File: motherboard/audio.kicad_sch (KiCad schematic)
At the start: 1 part, among them U23 TPA2028D1YZFT

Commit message: audio done
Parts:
- added C71, C72: 0.1uF, Capacitor_SMD:C_0402_1005Metric, symbol Device:C_Small
- added C73, C75, C76, C78, C79: 1uF, Capacitor_SMD:C_0402_1005Metric, symbol Device:C_Small
- added C74, C77: 10uF, Capacitor_SMD:C_0402_1005Metric, symbol Device:C_Small
- added CN1: PJ-332A-6A (3.5mm Jack), Headphone_Jack:AUDIO-SMD_PJ-332A-6A, symbol Headphone_Jack:PJ-332A-6A
- added D6, D7: LESD8D5.0CB1T5G, Diode_SMD:D_SOD-882, symbol Device:D_TVS_Small_Filled
- added J3: RIGHT SPEAKERS, symbol Connector_Generic:Conn_01x02
- added J4: LEFT SPEAKERS, symbol Connector_Generic:Conn_01x02
- added Q12: 2SK3018W, Package_TO_SOT_SMD:SOT-323_SC-70, symbol Transistor_FET:BSS214NW
- added R102, R103, R104: 0R, Resistor_SMD:R_0402_1005Metric, symbol Device:R_Small
- added R105, R106, R110: 10k, Resistor_SMD:R_0402_1005Metric, symbol Device:R_Small
- added R107, R108: 33R, Resistor_SMD:R_0402_1005Metric, symbol Device:R_Small
- added R109: 100k, Resistor_SMD:R_0402_1005Metric, symbol Device:R_Small
- added R111: 2.2k, Resistor_SMD:R_0402_1005Metric, symbol Device:R_Small
- added U25: TPA2028D1YZFT, TPA2028D1YZFT:BGA9C50P3X3_162X162X63, symbol Audio_Amp:TPA2028D1YZFT
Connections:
- net GND: now reaches U23.A1 (PGND)
- net GND: now also C73.2, C74.2, C76.1, C77.2, C79.1, D6.1 (A1), D7.1 (A1), Q12.2 (S), U25.A1 (PGND)
- net R_AMP_SCL: now reaches U23.A2 (SCL)
- net R_AMP_SDA: now reaches U23.A3 (SDA)
- net at U23.B1 (OUT+): now also J3.1 (Pin_1)
- net SPK_EN: now reaches U23.B2 (EN)
- net SPK_EN: now also U25.B2 (EN)
- net at U23.B3 (IN+): now also C75.2
- net at U23.C1 (OUT-): now also J3.2 (Pin_2)
- net +5V: now reaches U23.C2 (PVDD)
- net +5V: now also C74.1, C77.1, U25.C2 (PVDD)
- net at U23.C3 (IN-): now also C76.2
- new net: C72.2, R107.2
- new net: C73.1, Q12.1 (G), R110.1
- new net: J4.1 (Pin_1), U25.B1 (OUT+)
- new net: C78.2, U25.B3 (IN+)
- new net: J4.2 (Pin_2), U25.C1 (OUT-)
- new net: C79.2, U25.C3 (IN-)
- new net: C71.2, R108.2
- new net +1V8: R109.2, R111.2
- new net GND_AUDUO: CN1.2, R105.1, R106.1, R107.1, R108.1
- new net GPIO1_C4/HP_DET_L: Q12.3 (D), R111.1
- new net HPL: C72.1, R104.2, R106.2
- new net HPR: C71.1, R103.2, R105.2
- new net L_AMP_SCL: U25.A2 (SCL)
- new net L_AMP_SDA: U25.A3 (SDA)
- new net L_DET: CN1.5, CN1.6, R109.1, R110.2
- new net L_HP: C78.1, CN1.4, D7.2 (A2), R104.1
- new net MIC: CN1.1, R102.1
- new net MIC_IN: R102.2
- new net R_HP: C75.1, CN1.3, D6.2 (A2), R103.1

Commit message: motherboard schematic done
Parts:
- added R118, R119: 0R, Resistor_SMD:R_0402_1005Metric, symbol Device:R_Small
- J3, J4: footprint (none) -> Connector_PinHeader_2.54mm:PinHeader_1x02_P2.54mm_Horizontal
- U23, U25: footprint TPA2028D1YZFT:BGA9C50P3X3_162X162X63 -> Audio_Amp:BGA9C50P3X3_162X162X63
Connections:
- net HPL: now also C78.1
- net HPR: now also C75.1
- net L_HP: no longer C78.1
- net R_HP: no longer C75.1
- net SPK_EN: now also R118.1, R118.2, R119.1; no longer U25.B2 (EN)
- new net: R119.2, U25.B2 (EN)
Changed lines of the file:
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@@
 	(wire
 		(pts
-			(xy 151.13 134.62) (xy 161.29 134.62)
+			(xy 151.13 134.62) (xy 167.64 134.62)
 		)
 		(stroke
@@
 	(wire
 		(pts
-			(xy 80.01 81.28) (xy 87.63 81.28)
+			(xy 68.58 88.9) (xy 72.39 88.9)
 		)
 		(stroke
@@
 	(wire
 		(pts
+			(xy 81.28 81.28) (xy 87.63 81.28)
+		)
+		(stroke
+			(width 0)
+			(type default)
+		)
+	)
+	(wire
+		(pts
 			(xy 135.89 113.03) (xy 138.43 113.03)
 		)
@@
 	(wire
 		(pts
+			(xy 77.47 88.9) (xy 81.28 88.9)
+		)
+		(stroke
+			(width 0)
+			(type default)
+		)
+	)
+	(wire
+		(pts
 			(xy 88.9 127) (xy 99.06 127)
 		)
@@
 	(wire
 		(pts
-			(xy 156.21 127) (xy 161.29 127)
+			(xy 156.21 127) (xy 167.64 127)
 		)
 		(stroke
@@
 	(wire
 		(pts
+			(xy 81.28 88.9) (xy 81.28 81.28)
+		)
+		(stroke
+			(width 0)
+			(type default)
+		)
+	)
+	(wire
+		(pts
+			(xy 172.72 91.44) (xy 175.26 91.44)
+		)
+		(stroke
+			(width 0)
+			(type default)
+		)
+	)
+	(wire
+		(pts
 			(xy 132.08 134.62) (xy 151.13 134.62)
 		)
@@
 	(wire
 		(pts
+			(xy 175.26 85.09) (xy 179.07 85.09)
+		)
+		(stroke
+			(width 0)
+			(type default)
+		)
+	)
+	(wire
+		(pts
 			(xy 99.06 148.59) (xy 100.33 148.59)
 		)
@@
 	(wire
 		(pts
+			(xy 175.26 91.44) (xy 175.26 85.09)
+		)
+		(stroke
+			(width 0)
+			(type default)
+		)
+	)
+	(wire
+		(pts
 			(xy 88.9 129.54) (xy 95.25 129.54)
 		)
@@
 	(wire
 		(pts
-			(xy 171.45 85.09) (xy 179.07 85.09)
+			(xy 157.48 91.44) (xy 167.64 91.44)
 		)
 		(stroke
@@
 		)
 	)
-	(label "L_HP"
+	(label "L_AUDIO"
 		(at 160.02 77.47 0)
 		(fields_autoplaced yes)
@@
 		)
 	)
-	(label "R_HP"
-		(at 68.58 73.66 0)
+	(label "SPK_EN"
+		(at 157.48 91.44 0)
 		(fields_autoplaced yes)
 		(effects
@@
 		)
 	)
-	(label "SPK_EN"
-		(at 171.45 85.09 0)
+	(label "AGND"
+		(at 93.98 137.16 180)
 		(fields_autoplaced yes)
 		(effects
@@
 				(size 1.27 1.27)
 			)
-			(justify left bottom)
+			(justify right bottom)
 		)
 	)
-	(label "AGND"
-		(at 93.98 137.16 180)
+	(label "L_AUDIO"
+		(at 157.48 134.62 0)
 		(fields_autoplaced yes)
 		(effects
@@
 				(size 1.27 1.27)
 			)
-			(justify right bottom)
+			(justify left bottom)
 		)
 	)
@@
 	)
 	(label "SPK_EN"
-		(at 80.01 81.28 0)
+		(at 81.28 81.28 0)
+		(fields_autoplaced yes)
+		(effects
+			(font
+				(size 1.27 1.27)
+			)
+			(justify left bottom)
+		)
+	)
+	(label "R_AUDIO"
+		(at 157.48 127 0)
 		(fields_autoplaced yes)
 		(effects
@@
 		)
 	)
+	(label "R_AUDIO"
+		(at 68.58 73.66 0)
+		(fields_autoplaced yes)
+		(effects
+			(font
+				(size 1.27 1.27)
+			)
+			(justify left bottom)
+		)
+	)
 	(label "R_DET"
 		(at 111.76 111.76 0)
@@
 	(hierarchical_label "SPK_EN"
 		(shape input)
-		(at 80.01 81.28 180)
+		(at 68.58 88.9 180)
 		(fields_autoplaced yes)
 		(effects
@@
 	(hierarchical_label "HPR"
 		(shape input)
-		(at 161.29 127 0)
+		(at 167.64 127 0)
 		(fields_autoplaced yes)
 		(effects
@@
 	(hierarchical_label "HPL"
 		(shape input)
-		(at 161.29 134.62 0)
+		(at 167.64 134.62 0)
 		(fields_autoplaced yes)
 		(effects
@@
 			)
 		)
-		(property "Footprint" ""
+		(property "Footprint" "Connector_PinHeader_2.54mm:PinHeader_1x02_P2.54mm_Horizontal"
 			(at 125.73 68.58 0)
 			(effects
@@
 			)
 		)
-		(property "Footprint" "TPA2028D1YZFT:BGA9C50P3X3_162X162X63"
+		(property "Footprint" "Audio_Amp:BGA9C50P3X3_162X162X63"
 			(at 195.58 77.47 0)
 			(effects
@@
 			)
 		)
-		(property "Footprint" "TPA2028D1YZFT:BGA9C50P3X3_162X162X63"
+		(property "Footprint" "Audio_Amp:BGA9C50P3X3_162X162X63"
 			(at 104.14 73.66 0)
 			(effects
@@
 			)
 		)
-		(property "Footprint" ""
+		(property "Footprint" "Connector_PinHeader_2.54mm:PinHeader_1x02_P2.54mm_Horizontal"
 			(at 217.17 72.39 0)
 			(effects
@@
 	)
 	(symbol
+		(lib_id "Device:R_Small")
+		(at 170.18 91.44 90)
+		(unit 1)
+		(exclude_from_sim no)
+		(in_bom yes)
+		(on_board yes)
+		(dnp no)
+		(fields_autoplaced yes)
+		(property "Reference" "R119"
+			(at 170.18 86.36 90)
+			(effects
+				(font
+					(size 1.27 1.27)
+				)
+			)
+		)
+		(property "Value" "0R"
+			(at 170.18 88.9 90)
+			(effects
+				(font
+					(size 1.27 1.27)
+				)
+			)
+		)
+		(property "Footprint" "Resistor_SMD:R_0402_1005Metric"
+			(at 170.18 91.44 0)
+			(effects
+				(font
+					(size 1.27 1.27)
+				)
+				(hide yes)
+			)
+		)
+		(property "Datasheet" "~"
+			(at 170.18 91.44 0)
+			(effects
+				(font
+					(size 1.27 1.27)
+				)
+				(hide yes)
+			)
+		)
+		(property "Description" "Resistor, small symbol"
+			(at 170.18 91.44 0)
+			(effects
+				(font
+					(size 1.27 1.27)
+				)
+				(hide yes)
+			)
+		)
+		(pin "1"
+		)
+		(pin "2"
+		)
+		(instances
+			(project "motherboard"
+				(path "/025fe4d1-0305-4b34-be04-f8d9818125a4/d168cefe-cdbf-401a-9d73-1a46286dd06c"
+					(reference "R119")
+					(unit 1)
+				)
+			)
+		)
+	)
+	(symbol
 		(lib_id "power:GND")
 		(at 160.02 80.01 0)
@@
 					(unit 1)
 				)
+			)
+		)
+	)
+	(symbol
+		(lib_id "Device:R_Small")
+		(at 74.93 88.9 90)
+		(unit 1)
+		(exclude_from_sim no)
+		(in_bom yes)
+		(on_board yes)
+		(dnp no)
+		(fields_autoplaced yes)
+		(property "Reference" "R118"
+			(at 74.93 83.82 90)
+			(effects
+				(font
+					(size 1.27 1.27)
+				)
+			)
+		)
+		(property "Value" "0R"
+			(at 74.93 86.36 90)
+			(effects
+				(font
+					(size 1.27 1.27)
+				)
+			)
+		)
+		(property "Footprint" "Resistor_SMD:R_0402_1005Metric"
+			(at 74.93 88.9 0)
+			(effects
+				(font
+					(size 1.27 1.27)
+				)
+				(hide yes)
+			)
+		)
+		(property "Datasheet" "~"
+			(at 74.93 88.9 0)
+			(effects
+				(font
+					(size 1.27 1.27)
+				)
+				(hide yes)
+			)
+		)
+		(property "Description" "Resistor, small symbol"
+			(at 74.93 88.9 0)
+			(effects
+				(font
+					(size 1.27 1.27)
+				)
+				(hide yes)
+			)
+		)
+		(pin "1"
+		)
+		(pin "2"
+		)
+		(instances
+			(project "motherboard"
+				(path "/025fe4d1-0305-4b34-be04-f8d9818125a4/d168cefe-cdbf-401a-9d73-1a46286dd06c"
+					(reference "R118")
+					(unit 1)
+				)

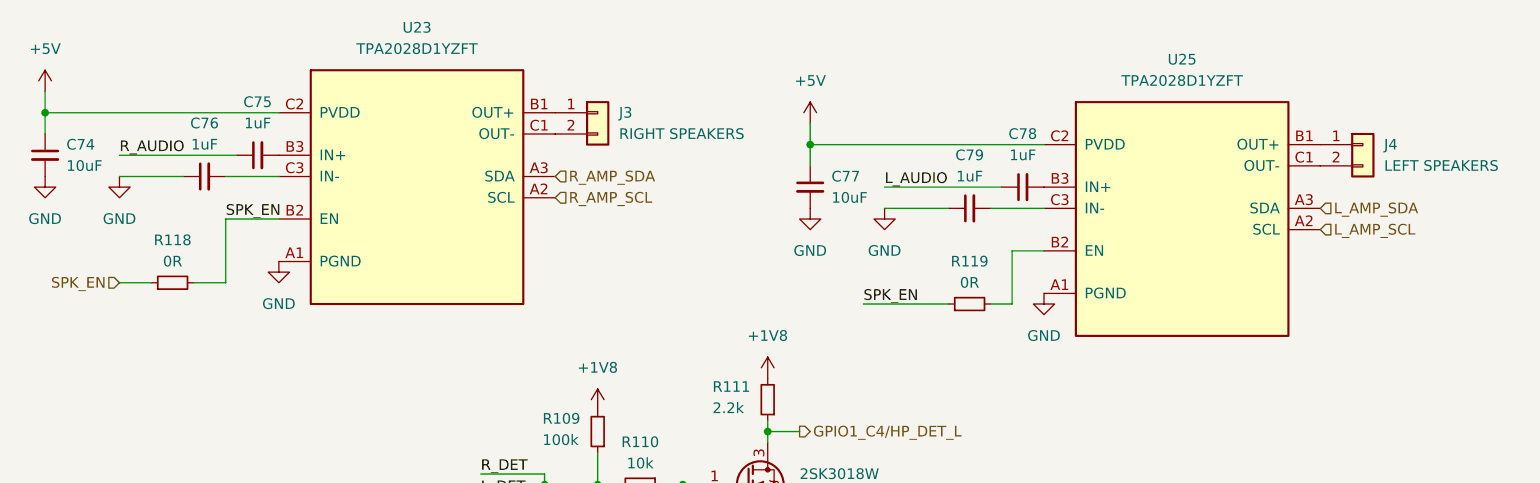
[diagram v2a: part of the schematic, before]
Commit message: placement roughly halfway done
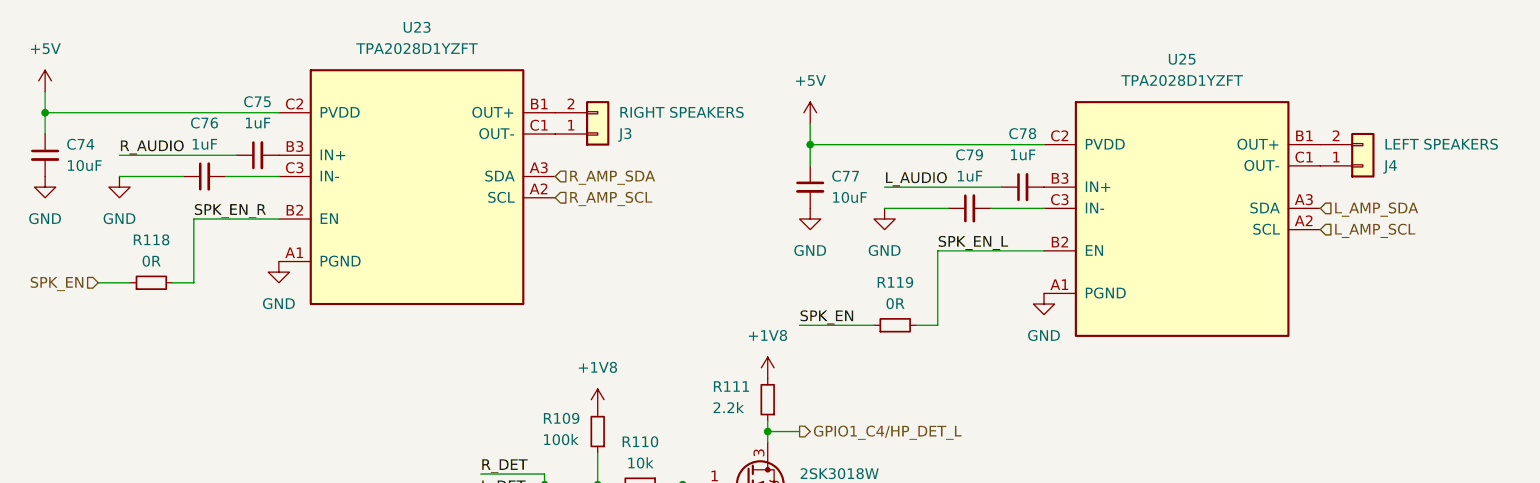
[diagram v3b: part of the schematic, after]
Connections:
- net SPK_EN: no longer R118.2, U23.B2 (EN)
- net at J3.1 (Pin_1): now also U23.C1 (OUT-); no longer U23.B1 (OUT+)
- net at J3.2 (Pin_2): now also U23.B1 (OUT+); no longer U23.C1 (OUT-)
- net at U25.B1 (OUT+): now also J4.2 (Pin_2); no longer J4.1 (Pin_1)
- net SPK_EN_L: now reaches R119.2, U25.B2 (EN)
- net at U25.C1 (OUT-): now also J4.1 (Pin_1); no longer J4.2 (Pin_2)
- new net SPK_EN_R: R118.2, U23.B2 (EN)
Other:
- moved on the sheet: R118, R119
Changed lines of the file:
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@@
 	(wire
 		(pts
+			(xy 77.47 81.28) (xy 77.47 88.9)
+		)
+		(stroke
+			(width 0)
+			(type default)
+		)
+	)
+	(wire
+		(pts
 			(xy 153.67 147.32) (xy 156.21 147.32)
 		)
@@
 	(wire
 		(pts
-			(xy 68.58 88.9) (xy 72.39 88.9)
+			(xy 77.47 88.9) (xy 74.93 88.9)
 		)
 		(stroke
@@
 	(wire
 		(pts
-			(xy 128.27 113.03) (xy 125.73 113.03)
+			(xy 66.04 88.9) (xy 69.85 88.9)
 		)
 		(stroke
@@
 	(wire
 		(pts
-			(xy 81.28 81.28) (xy 87.63 81.28)
+			(xy 128.27 113.03) (xy 125.73 113.03)
 		)
 		(stroke
@@
 	(wire
 		(pts
-			(xy 135.89 113.03) (xy 138.43 113.03)
+			(xy 77.47 81.28) (xy 87.63 81.28)
 		)
 		(stroke
@@
 	(wire
 		(pts
-			(xy 101.6 134.62) (xy 116.84 134.62)
+			(xy 135.89 113.03) (xy 138.43 113.03)
 		)
 		(stroke
@@
 	(wire
 		(pts
-			(xy 99.06 142.24) (xy 99.06 148.59)
+			(xy 101.6 134.62) (xy 116.84 134.62)
 		)
 		(stroke
@@
 	(wire
 		(pts
-			(xy 151.13 134.62) (xy 151.13 135.89)
+			(xy 99.06 142.24) (xy 99.06 148.59)
 		)
 		(stroke
@@
 	(wire
 		(pts
-			(xy 151.13 74.93) (xy 151.13 72.39)
+			(xy 151.13 134.62) (xy 151.13 135.89)
 		)
 		(stroke
@@
 	(wire
 		(pts
-			(xy 77.47 88.9) (xy 81.28 88.9)
+			(xy 151.13 74.93) (xy 151.13 72.39)
 		)
 		(stroke
@@
 	(wire
 		(pts
-			(xy 81.28 88.9) (xy 81.28 81.28)
-		)
-		(stroke
-			(width 0)
-			(type default)
-		)
-	)
-	(wire
-		(pts
-			(xy 172.72 91.44) (xy 175.26 91.44)
+			(xy 163.83 93.98) (xy 166.37 93.98)
 		)
 		(stroke
@@
 	(wire
 		(pts
-			(xy 175.26 85.09) (xy 179.07 85.09)
+			(xy 166.37 85.09) (xy 179.07 85.09)
 		)
 		(stroke
@@
 	(wire
 		(pts
-			(xy 175.26 91.44) (xy 175.26 85.09)
+			(xy 166.37 93.98) (xy 166.37 85.09)
 		)
 		(stroke
@@
 	(wire
 		(pts
-			(xy 157.48 91.44) (xy 167.64 91.44)
+			(xy 134.62 142.24) (xy 134.62 140.97)
 		)
 		(stroke
@@
 	(wire
 		(pts
-			(xy 134.62 142.24) (xy 134.62 140.97)
+			(xy 121.92 127) (xy 134.62 127)
 		)
 		(stroke
@@
 	(wire
 		(pts
-			(xy 121.92 127) (xy 134.62 127)
+			(xy 149.86 93.98) (xy 158.75 93.98)
 		)
 		(stroke
@@
 	)
 	(label "SPK_EN"
-		(at 157.48 91.44 0)
+		(at 149.86 93.98 0)
 		(fields_autoplaced yes)
 		(effects
@@
 		)
 	)
-	(label "SPK_EN"
-		(at 81.28 81.28 0)
+	(label "SPK_EN_R"
+		(at 77.47 81.28 0)
 		(fields_autoplaced yes)
 		(effects
@@
 		)
 	)
+	(label "SPK_EN_L"
+		(at 166.37 85.09 0)
+		(fields_autoplaced yes)
+		(effects
+			(font
+				(size 1.27 1.27)
+			)
+			(justify left bottom)
+		)
+	)
 	(label "R_DET"
 		(at 111.76 111.76 0)
@@
 	(hierarchical_label "SPK_EN"
 		(shape input)
-		(at 68.58 88.9 180)
+		(at 66.04 88.9 180)
 		(fields_autoplaced yes)
 		(effects
@@
 	(symbol
 		(lib_id "Connector_Generic:Conn_01x02")
-		(at 125.73 68.58 0)
+		(at 125.73 71.12 0)
+		(mirror x)
 		(unit 1)
 		(exclude_from_sim no)
@@
 		(on_board yes)
 		(dnp no)
-		(fields_autoplaced yes)
 		(property "Reference" "J3"
-			(at 128.27 68.5799 0)
+			(at 128.27 71.1201 0)
 			(effects
 				(font
@@
 		)
 		(property "Value" "RIGHT SPEAKERS"
-			(at 128.27 71.1199 0)
+			(at 128.27 68.5801 0)
 			(effects
 				(font
@@
 		)
 		(property "Footprint" "Connector_PinHeader_2.54mm:PinHeader_1x02_P2.54mm_Horizontal"
-			(at 125.73 68.58 0)
+			(at 125.73 71.12 0)
 			(effects
 				(font
@@
 		)
 		(property "Datasheet" "~"
-			(at 125.73 68.58 0)
+			(at 125.73 71.12 0)
 			(effects
 				(font
@@
 		)
 		(property "Description" "Generic connector, single row, 01x02, script generated (kicad-library-utils/schlib/autogen/connector/)"
-			(at 125.73 68.58 0)
+			(at 125.73 71.12 0)
 			(effects
 				(font
@@
 	(symbol
 		(lib_id "Connector_Generic:Conn_01x02")
-		(at 217.17 72.39 0)
+		(at 217.17 74.93 0)
+		(mirror x)
 		(unit 1)
 		(exclude_from_sim no)
@@
 		(on_board yes)
 		(dnp no)
-		(fields_autoplaced yes)
 		(property "Reference" "J4"
-			(at 219.71 72.3899 0)
+			(at 219.71 74.9301 0)
 			(effects
 				(font
@@
 		)
 		(property "Value" "LEFT SPEAKERS"
-			(at 219.71 74.9299 0)
+			(at 219.71 72.3901 0)
 			(effects
 				(font
@@
 		)
 		(property "Footprint" "Connector_PinHeader_2.54mm:PinHeader_1x02_P2.54mm_Horizontal"
-			(at 217.17 72.39 0)
+			(at 217.17 74.93 0)
 			(effects
 				(font
@@
 		)
 		(property "Datasheet" "~"
-			(at 217.17 72.39 0)
+			(at 217.17 74.93 0)
 			(effects
 				(font
@@
 		)
 		(property "Description" "Generic connector, single row, 01x02, script generated (kicad-library-utils/schlib/autogen/connector/)"
-			(at 217.17 72.39 0)
+			(at 217.17 74.93 0)
 			(effects
 				(font
@@
 	(symbol
 		(lib_id "Device:R_Small")
-		(at 170.18 91.44 90)
+		(at 161.29 93.98 90)
 		(unit 1)
 		(exclude_from_sim no)
@@
 		(fields_autoplaced yes)
 		(property "Reference" "R119"
-			(at 170.18 86.36 90)
+			(at 161.29 88.9 90)
 			(effects
 				(font
@@
 		)
 		(property "Value" "0R"
-			(at 170.18 88.9 90)
+			(at 161.29 91.44 90)
 			(effects
 				(font
@@
 		)
 		(property "Footprint" "Resistor_SMD:R_0402_1005Metric"
-			(at 170.18 91.44 0)
+			(at 161.29 93.98 0)
 			(effects
 				(font
@@
 		)
 		(property "Datasheet" "~"
-			(at 170.18 91.44 0)
+			(at 161.29 93.98 0)
 			(effects
 				(font
@@
 		)
 		(property "Description" "Resistor, small symbol"
-			(at 170.18 91.44 0)
+			(at 161.29 93.98 0)
 			(effects
 				(font
@@
 	(symbol
 		(lib_id "Device:R_Small")
-		(at 74.93 88.9 90)
+		(at 72.39 88.9 90)
 		(unit 1)
 		(exclude_from_sim no)
@@
 		(fields_autoplaced yes)
 		(property "Reference" "R118"
-			(at 74.93 83.82 90)
+			(at 72.39 83.82 90)
 			(effects
 				(font
@@
 		)
 		(property "Value" "0R"
-			(at 74.93 86.36 90)
+			(at 72.39 86.36 90)
 			(effects
 				(font
@@
 		)
 		(property "Footprint" "Resistor_SMD:R_0402_1005Metric"
-			(at 74.93 88.9 0)
+			(at 72.39 88.9 0)
 			(effects
 				(font
@@
 		)
 		(property "Datasheet" "~"
-			(at 74.93 88.9 0)
+			(at 72.39 88.9 0)
 			(effects
 				(font
@@
 		)
 		(property "Description" "Resistor, small symbol"
-			(at 74.93 88.9 0)
+			(at 72.39 88.9 0)
 			(effects
 				(font

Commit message: layout nearing completion
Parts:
- C74, C77: footprint Capacitor_SMD:C_0402_1005Metric -> Capacitor_SMD:C_0603_1608Metric
- J3, J4: footprint Connector_PinHeader_2.54mm:PinHeader_1x02_P2.54mm_Horizontal -> Connector_PinHeader_2.54mm:PinHeader_1x02_P2.54mm_Vertical
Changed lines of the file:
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@@
 			)
 		)
-		(property "Footprint" "Connector_PinHeader_2.54mm:PinHeader_1x02_P2.54mm_Horizontal"
+		(property "Footprint" "Connector_PinHeader_2.54mm:PinHeader_1x02_P2.54mm_Vertical"
 			(at 125.73 71.12 0)
 			(effects
@@
 			)
 		)
-		(property "Footprint" "Capacitor_SMD:C_0402_1005Metric"
+		(property "Footprint" "Capacitor_SMD:C_0603_1608Metric"
 			(at 151.13 77.47 0)
 			(effects
@@
 			)
 		)
-		(property "Footprint" "Capacitor_SMD:C_0402_1005Metric"
+		(property "Footprint" "Capacitor_SMD:C_0603_1608Metric"
 			(at 59.69 73.66 0)
 			(effects
@@
 			)
 		)
-		(property "Footprint" "Connector_PinHeader_2.54mm:PinHeader_1x02_P2.54mm_Horizontal"
+		(property "Footprint" "Connector_PinHeader_2.54mm:PinHeader_1x02_P2.54mm_Vertical"
 			(at 217.17 74.93 0)
 			(effects

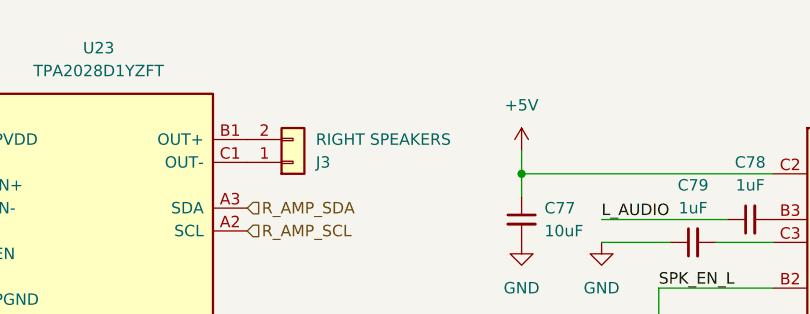
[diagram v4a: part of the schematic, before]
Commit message: created display evaluation board + layout modifications
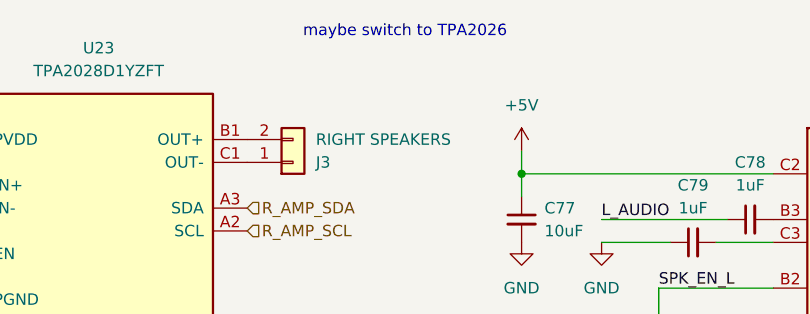
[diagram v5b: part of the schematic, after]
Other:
- note added: "maybe switch to TPA2026"
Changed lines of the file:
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@@
 	(generator_version "8.99")
 	(paper "A4")
+	(text "maybe switch to TPA2026"
+		(exclude_from_sim no)
+		(at 138.176 56.642 0)
+		(effects
+			(font
+				(size 1.27 1.27)
+			)
+		)
+	)
 	(junction
 		(at 59.69 68.58)
